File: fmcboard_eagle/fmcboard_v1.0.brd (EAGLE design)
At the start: 98 x 74 mm, 50 parts, among them IC1 OPA699ID, IC2 OPA699ID, IC3 ICL7660CPA, IC4 ICL7660CPA, J1 8pin, J12 4p-2.54, J2 ASP-134604-01, J3 4p-2.54, J4 4p-2.54, J5 8pin, U1 TXS0108EPWR

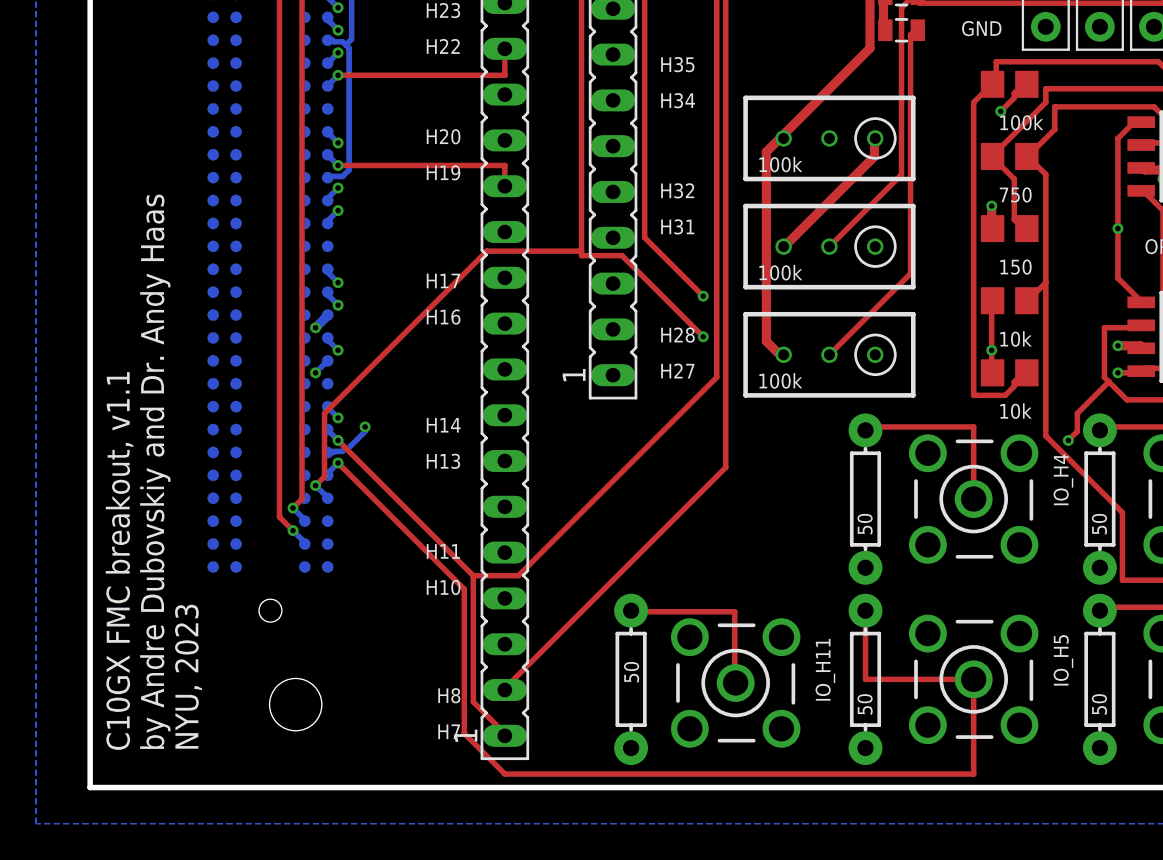
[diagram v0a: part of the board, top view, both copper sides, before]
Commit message: Change resistors and labels
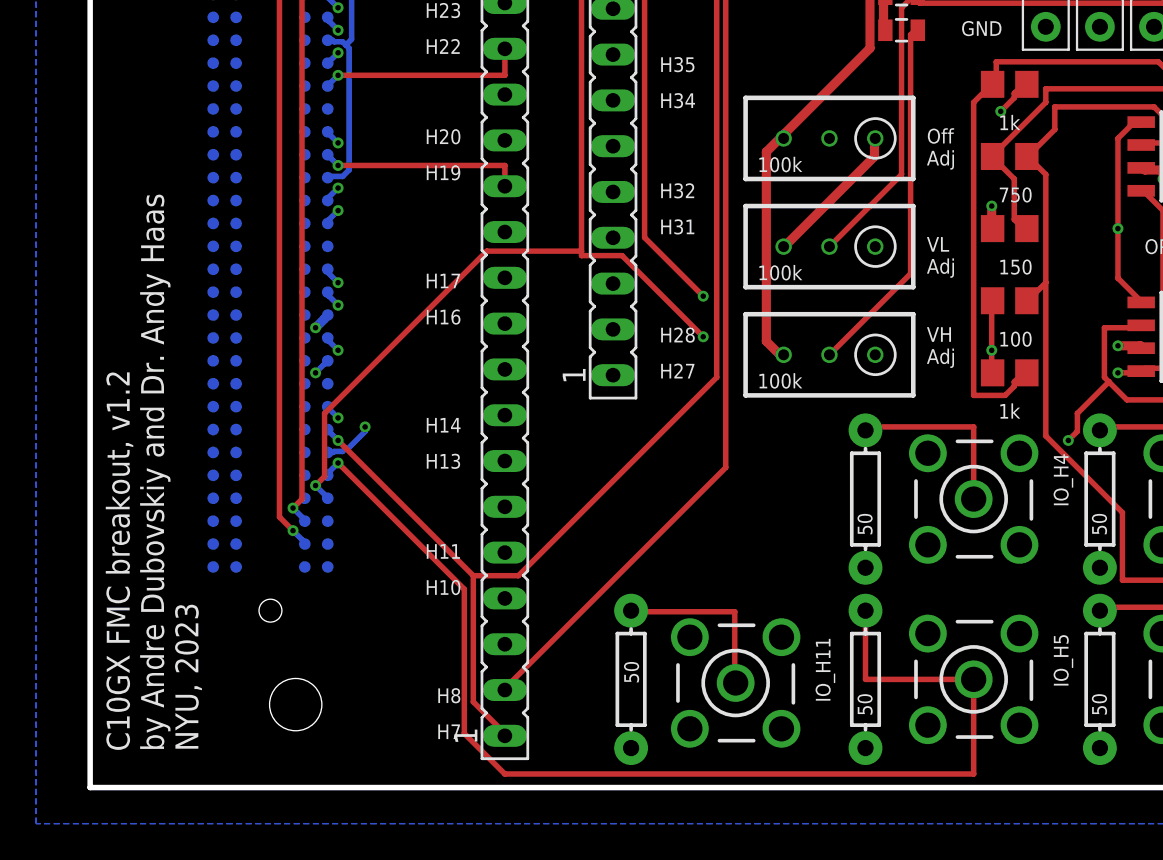
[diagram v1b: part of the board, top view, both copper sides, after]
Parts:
- R13: value 10k -> 100
- R14: value 10k -> 1k
- R3: value 100k -> 1k
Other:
- board text added: "C10GX FMC breakout, v1.2 by Andre Dubovskiy and Dr. Andy Haas NYU, 2023"
- board text added: "Off Adj"
- board text added: "VH Adj"
- board text added: "VL Adj"
- board text removed: "C10GX FMC breakout, v1.1 by Andre Dubovskiy and Dr. Andy Haas NYU, 2023"
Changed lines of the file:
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@@
 <?xml version="1.0" encoding="utf-8"?>
 <!DOCTYPE eagle SYSTEM "eagle.dtd">
-<eagle version="9.5.2">
+<eagle version="9.6.2">
 <drawing>
 <settings>
-<setting alwaysvectorfont="yes"/>
+<setting alwaysvectorfont="no"/>
 <setting verticaltext="up"/>
 </settings>
@@
 <text x="92.6" y="27.5" size="0.8128" layer="21" rot="R180">OPIN</text>
 <text x="92.6" y="52.5" size="0.8128" layer="21" rot="R180">GND</text>
-<text x="6" y="2" size="1.27" layer="21" rot="R90">C10GX FMC breakout, v1.1
+<text x="6" y="2" size="1.27" layer="21" rot="R90">C10GX FMC breakout, v1.2
 by Andre Dubovskiy and Dr. Andy Haas
 NYU, 2023</text>
@@
 <text x="33.6" y="53.5" size="0.8128" layer="21" rot="R180">H4</text>
 <text x="33.6" y="55.5" size="0.8128" layer="21" rot="R180">H5</text>
+<text x="46.4" y="23.5" size="0.8128" layer="21">VH
+Adj</text>
+<text x="46.4" y="28.5" size="0.8128" layer="21">VL
+Adj</text>
+<text x="46.4" y="34.5" size="0.8128" layer="21">Off
+Adj</text>
 </plain>
 <attributes>
@@
 <attribute name="VALUE" x="50.365" y="28.46" size="0.8128" layer="21"/>
 </element>
-<element name="R13" library="rcl" library_urn="urn:adsk.eagle:library:334" package="R0805" package3d_urn="urn:adsk.eagle:package:23553/2" value="10k" x="51" y="27" smashed="yes">
+<element name="R13" library="rcl" library_urn="urn:adsk.eagle:library:334" package="R0805" package3d_urn="urn:adsk.eagle:package:23553/2" value="100" x="51" y="27" smashed="yes">
 <attribute name="POPULARITY" value="85" x="51" y="27" size="1.778" layer="27" display="off"/>
 <attribute name="SPICEPREFIX" value="R" x="51" y="27" size="1.778" layer="27" display="off"/>
 <attribute name="VALUE" x="50.365" y="24.46" size="0.8128" layer="21"/>
 </element>
-<element name="R14" library="rcl" library_urn="urn:adsk.eagle:library:334" package="R0805" package3d_urn="urn:adsk.eagle:package:23553/2" value="10k" x="51" y="23" smashed="yes">
+<element name="R14" library="rcl" library_urn="urn:adsk.eagle:library:334" package="R0805" package3d_urn="urn:adsk.eagle:package:23553/2" value="1k" x="51" y="23" smashed="yes">
 <attribute name="POPULARITY" value="85" x="51" y="23" size="1.778" layer="27" display="off"/>
 <attribute name="SPICEPREFIX" value="R" x="51" y="23" size="1.778" layer="27" display="off"/>
@@
 <attribute name="VALUE" x="39.5" y="34.95" size="0.8128" layer="21" rot="R180"/>
 </element>
-<element name="R3" library="rcl" library_urn="urn:adsk.eagle:library:334" package="R0805" package3d_urn="urn:adsk.eagle:package:23553/2" value="100k" x="51" y="39" smashed="yes">
+<element name="R3" library="rcl" library_urn="urn:adsk.eagle:library:334" package="R0805" package3d_urn="urn:adsk.eagle:package:23553/2" value="1k" x="51" y="39" smashed="yes">
 <attribute name="POPULARITY" value="85" x="51" y="39" size="1.778" layer="27" display="off"/>
 <attribute name="SPICEPREFIX" value="R" x="51" y="39" size="1.778" layer="27" display="off"/>

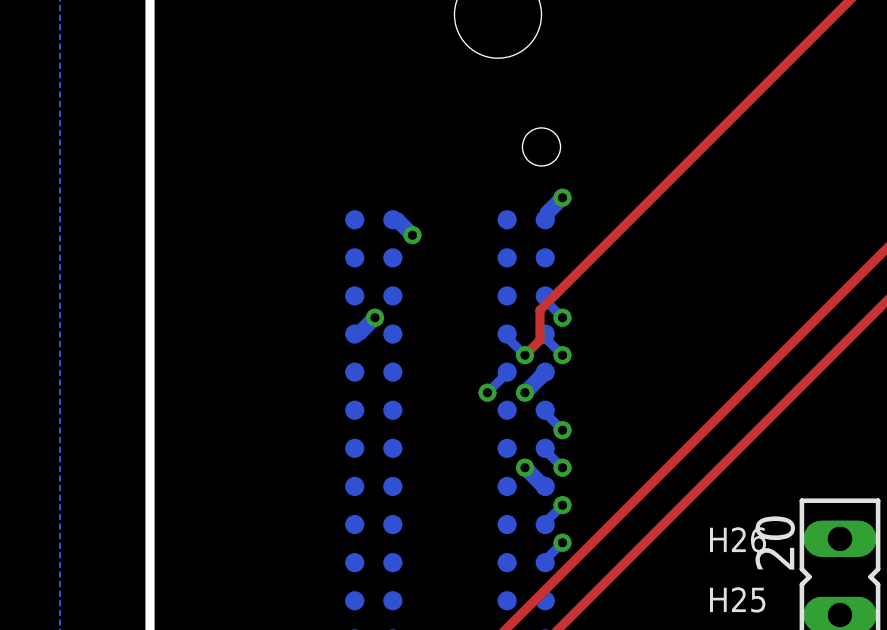
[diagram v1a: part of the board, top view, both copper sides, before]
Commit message: Add more power connections to FMC header
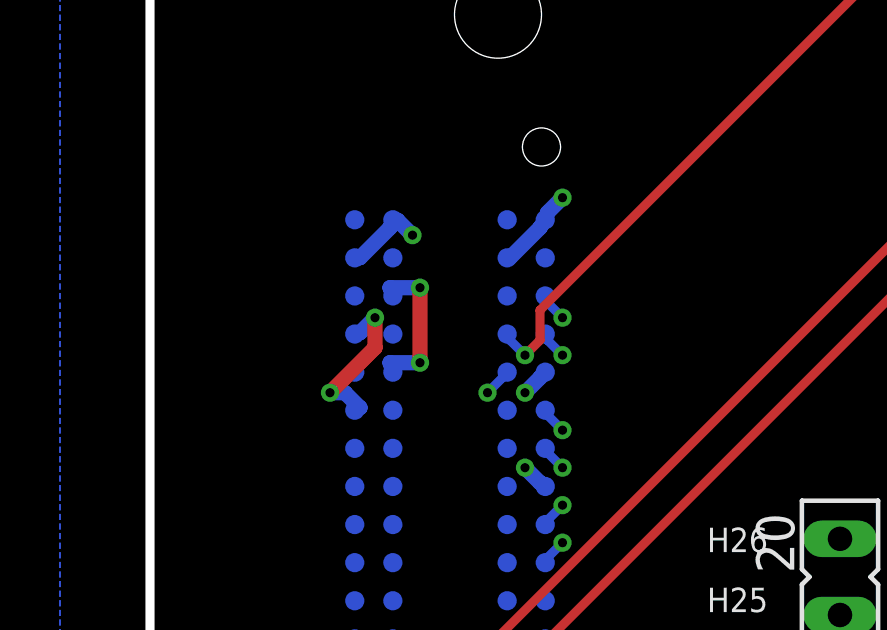
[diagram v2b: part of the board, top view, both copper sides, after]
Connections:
- net 12V: now also J2.C35
- net 1V8: now also J2.G39
- net 3V3: now also J2.C39, J2.D36, J2.D38
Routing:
- net 3V3: track 67.9 -> 76.6 mm, vias 1 -> 3
- net 12V: track 64.5 -> 69.0 mm, vias 1 -> 2
- net 1V8: track 94.3 -> 96.1 mm
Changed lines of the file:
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@@
 <layers>
 <layer number="1" name="top" color="4" fill="1" visible="yes" active="yes"/>
-<layer number="2" name="topgnd" color="16" fill="1" visible="no" active="yes"/>
+<layer number="2" name="topgnd" color="16" fill="1" visible="yes" active="yes"/>
 <layer number="3" name="Route3" color="4" fill="3" visible="no" active="no"/>
 <layer number="4" name="Route4" color="1" fill="4" visible="no" active="no"/>
@@
 <via x="31" y="62.25" extent="1-16" drill="0.3048"/>
 <via x="43.25" y="63.5" extent="1-16" drill="0.3048"/>
+<contactref element="J2" pad="G39"/>
+<wire x1="13" y1="61.5" x2="12" y2="60.5" width="0.508" layer="16"/>
+<wire x1="12" y1="60.5" x2="11.905" y2="60.495" width="0.508" layer="16"/>
+<wire x1="13" y1="61.5" x2="13.175" y2="61.765" width="0.508" layer="16"/>
 </signal>
 <signal name="3V3" class="1">
@@
 <contactref element="C13" pad="1"/>
 <wire x1="8.75" y1="61.25" x2="8.25" y2="61.75" width="0.508" layer="16"/>
-<wire x1="27.25" y1="61.25" x2="8.75" y2="61.25" width="0.508" layer="15"/>
+<wire x1="27.25" y1="61.25" x2="9" y2="61.25" width="0.508" layer="15"/>
+<wire x1="9" y1="61.25" x2="8.75" y2="61.25" width="0.508" layer="15"/>
 <wire x1="29" y1="59.5" x2="27.25" y2="61.25" width="0.508" layer="15"/>
 <wire x1="35" y1="59.5" x2="29" y2="59.5" width="0.508" layer="15"/>
@@
 <wire x1="56.25" y1="47.25" x2="56" y2="47.27" width="0.508" layer="15"/>
 <via x="8.75" y="61.25" extent="1-16" drill="0.3048"/>
+<contactref element="J2" pad="C39"/>
+<contactref element="J2" pad="D38"/>
+<contactref element="J2" pad="D36"/>
+<wire x1="9" y1="57" x2="8" y2="57" width="0.508" layer="16"/>
+<wire x1="9" y1="59.5" x2="9" y2="57" width="0.508" layer="1"/>
+<wire x1="9" y1="61.25" x2="9" y2="59.5" width="0.508" layer="15"/>
+<wire x1="8" y1="57" x2="8.095" y2="56.685" width="0.508" layer="16"/>
+<wire x1="9" y1="59.5" x2="8" y2="59.5" width="0.508" layer="16"/>
+<wire x1="8" y1="59.5" x2="8.095" y2="59.225" width="0.508" layer="16"/>
+<wire x1="8" y1="61.5" x2="7" y2="60.5" width="0.508" layer="16"/>
+<wire x1="7" y1="60.5" x2="6.825" y2="60.495" width="0.508" layer="16"/>
+<wire x1="8" y1="61.5" x2="8.095" y2="61.765" width="0.508" layer="16"/>
+<via x="9" y="57" extent="1-16" drill="0.3048"/>
+<via x="9" y="59.5" extent="1-16" drill="0.3048"/>
 </signal>
 <signal name="12V" class="1">
@@
 <wire x1="56.25" y1="50" x2="56" y2="49.81" width="0.508" layer="1"/>
 <via x="7.5" y="58.5" extent="1-16" drill="0.3048"/>
+<contactref element="J2" pad="C35"/>
+<wire x1="6.5" y1="56" x2="7" y2="55.5" width="0.508" layer="16"/>
+<wire x1="6" y1="56" x2="6.5" y2="56" width="0.508" layer="16"/>
+<wire x1="7.5" y1="57.5" x2="6" y2="56" width="0.508" layer="1"/>
+<wire x1="7.5" y1="58.5" x2="7.5" y2="57.5" width="0.508" layer="1"/>
+<wire x1="7" y1="55.5" x2="6.825" y2="55.415" width="0.508" layer="16"/>
+<via x="6" y="56" extent="1-16" drill="0.3048"/>
 </signal>
 <signal name="OPBUF1">

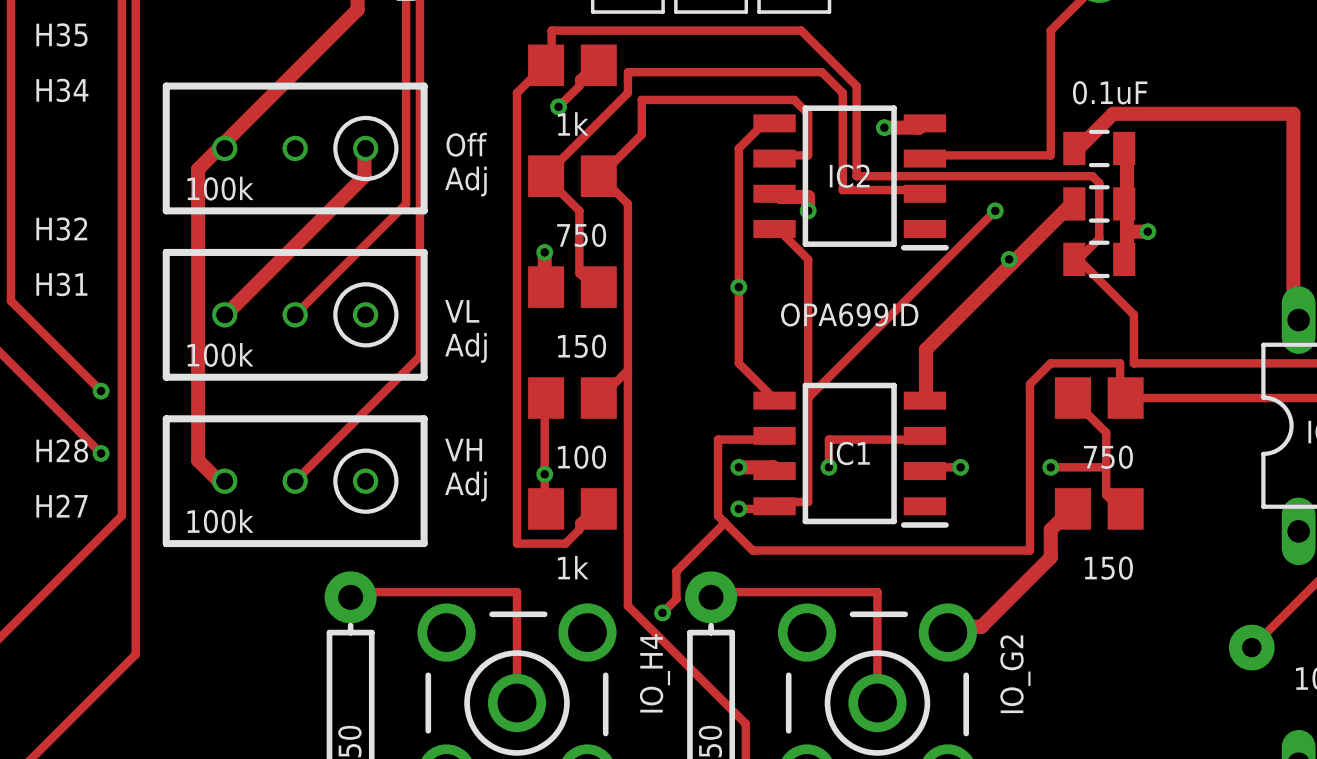
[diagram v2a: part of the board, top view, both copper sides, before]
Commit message: Update resistor values
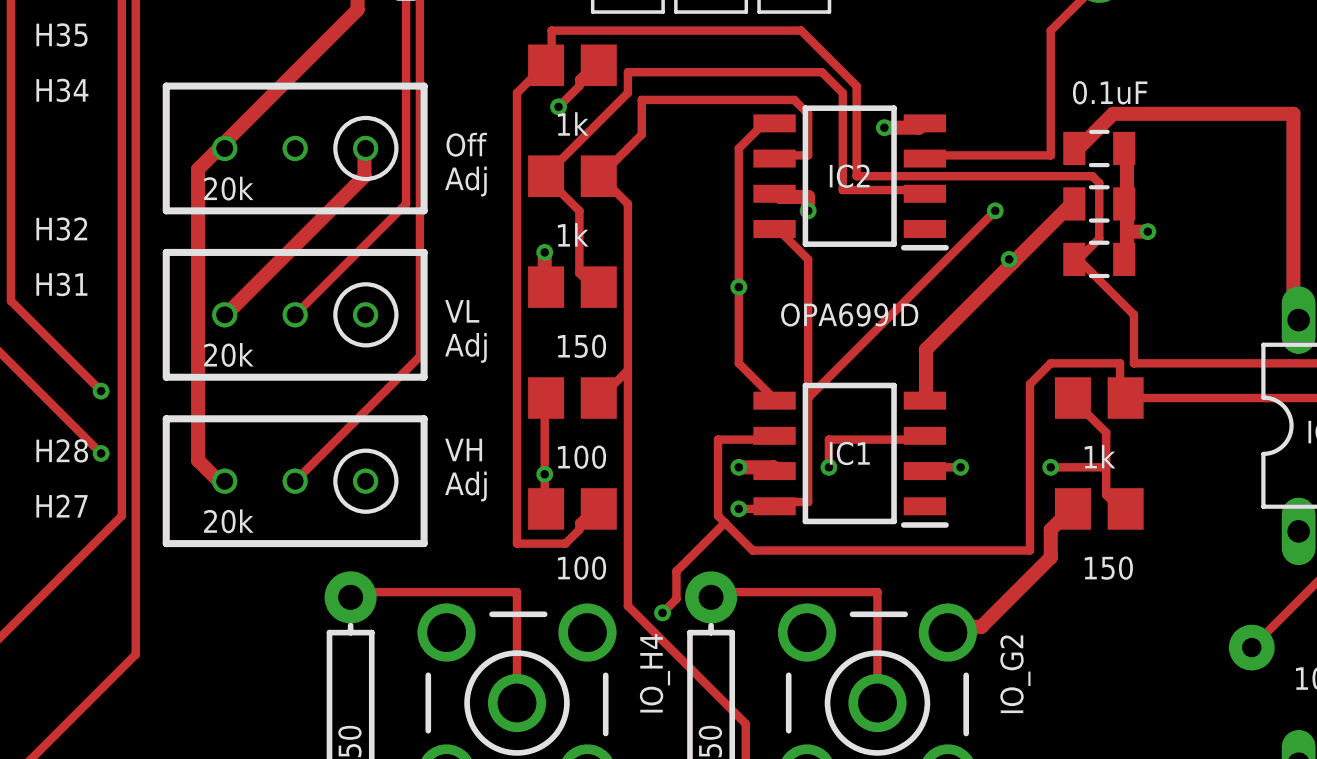
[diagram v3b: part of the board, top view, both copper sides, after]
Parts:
- R1, R7, R8: value 100k -> 20k
- R11, R9: value 750 -> 1k
- R14: value 1k -> 100
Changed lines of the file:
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@@
 <layers>
 <layer number="1" name="top" color="4" fill="1" visible="yes" active="yes"/>
-<layer number="2" name="topgnd" color="16" fill="1" visible="yes" active="yes"/>
+<layer number="2" name="topgnd" color="16" fill="1" visible="no" active="yes"/>
 <layer number="3" name="Route3" color="4" fill="3" visible="no" active="no"/>
 <layer number="4" name="Route4" color="1" fill="4" visible="no" active="no"/>
@@
 <attribute name="VALUE" x="29.619" y="7.032" size="0.8128" layer="21" rot="R270"/>
 </element>
-<element name="R7" library="resistor" library_urn="urn:adsk.eagle:library:348" package="RTRIM3296W" package3d_urn="urn:adsk.eagle:package:26033/1" value="100k" x="41" y="24" smashed="yes" rot="R90">
+<element name="R7" library="resistor" library_urn="urn:adsk.eagle:library:348" package="RTRIM3296W" package3d_urn="urn:adsk.eagle:package:26033/1" value="20k" x="41" y="24" smashed="yes" rot="R90">
 <attribute name="VALUE" x="39.5" y="22.95" size="0.8128" layer="21" rot="R180"/>
 </element>
-<element name="R8" library="resistor" library_urn="urn:adsk.eagle:library:348" package="RTRIM3296W" package3d_urn="urn:adsk.eagle:package:26033/1" value="100k" x="41" y="30" smashed="yes" rot="R90">
+<element name="R8" library="resistor" library_urn="urn:adsk.eagle:library:348" package="RTRIM3296W" package3d_urn="urn:adsk.eagle:package:26033/1" value="20k" x="41" y="30" smashed="yes" rot="R90">
 <attribute name="VALUE" x="39.5" y="28.95" size="0.8128" layer="21" rot="R180"/>
 </element>
@@
 <attribute name="VALUE" x="84.78" y="66.54" size="1.27" layer="21" font="vector" rot="R180"/>
 </element>
-<element name="R9" library="rcl" library_urn="urn:adsk.eagle:library:334" package="R0805" package3d_urn="urn:adsk.eagle:package:23553/2" value="750" x="70" y="27" smashed="yes">
+<element name="R9" library="rcl" library_urn="urn:adsk.eagle:library:334" package="R0805" package3d_urn="urn:adsk.eagle:package:23553/2" value="1k" x="70" y="27" smashed="yes">
 <attribute name="POPULARITY" value="85" x="70" y="27" size="1.778" layer="27" display="off"/>
 <attribute name="SPICEPREFIX" value="R" x="70" y="27" size="1.778" layer="27" display="off"/>
@@
 <attribute name="VALUE" x="69.365" y="20.46" size="0.8128" layer="21"/>
 </element>
-<element name="R11" library="rcl" library_urn="urn:adsk.eagle:library:334" package="R0805" package3d_urn="urn:adsk.eagle:package:23553/2" value="750" x="51" y="35" smashed="yes">
+<element name="R11" library="rcl" library_urn="urn:adsk.eagle:library:334" package="R0805" package3d_urn="urn:adsk.eagle:package:23553/2" value="1k" x="51" y="35" smashed="yes">
 <attribute name="POPULARITY" value="85" x="51" y="35" size="1.778" layer="27" display="off"/>
 <attribute name="SPICEPREFIX" value="R" x="51" y="35" size="1.778" layer="27" display="off"/>
@@
 <attribute name="VALUE" x="50.365" y="24.46" size="0.8128" layer="21"/>
 </element>
-<element name="R14" library="rcl" library_urn="urn:adsk.eagle:library:334" package="R0805" package3d_urn="urn:adsk.eagle:package:23553/2" value="1k" x="51" y="23" smashed="yes">
+<element name="R14" library="rcl" library_urn="urn:adsk.eagle:library:334" package="R0805" package3d_urn="urn:adsk.eagle:package:23553/2" value="100" x="51" y="23" smashed="yes">
 <attribute name="POPULARITY" value="85" x="51" y="23" size="1.778" layer="27" display="off"/>
 <attribute name="SPICEPREFIX" value="R" x="51" y="23" size="1.778" layer="27" display="off"/>
 <attribute name="VALUE" x="50.365" y="20.46" size="0.8128" layer="21"/>
 </element>
-<element name="R1" library="resistor" library_urn="urn:adsk.eagle:library:348" package="RTRIM3296W" package3d_urn="urn:adsk.eagle:package:26033/1" value="100k" x="41" y="36" smashed="yes" rot="R90">
+<element name="R1" library="resistor" library_urn="urn:adsk.eagle:library:348" package="RTRIM3296W" package3d_urn="urn:adsk.eagle:package:26033/1" value="20k" x="41" y="36" smashed="yes" rot="R90">
 <attribute name="VALUE" x="39.5" y="34.95" size="0.8128" layer="21" rot="R180"/>
 </element>
